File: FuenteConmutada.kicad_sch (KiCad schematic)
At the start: 25 parts, among them J1 Conn_01x02_Socket, J2 Conn_01x03_Socket, U1 MT3608

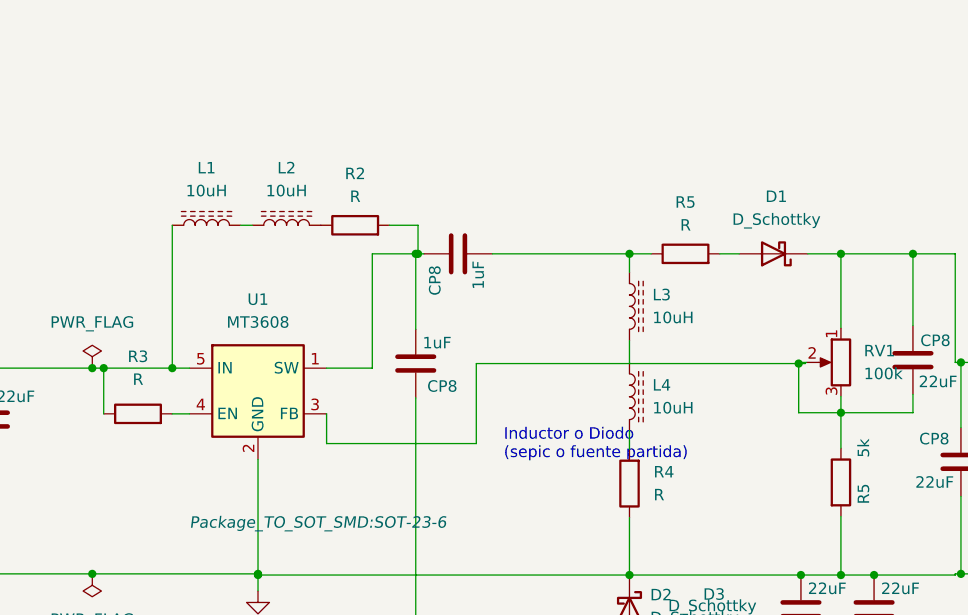
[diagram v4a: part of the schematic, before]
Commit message: Ajustes planos y tracks
Agrandar Margen a 40mils de los planos
Cambiar Rmed de lado del inductor (hacia Vin)
Cambiar Pos Inductores, mas cerca de SW
Aumentar a 50mils todos los tracks que no esten embutidos en planos
Puente en GND/Vfedback para no pasar debajo del SOT23
-Verificar cambios y poner Listo en la wiki
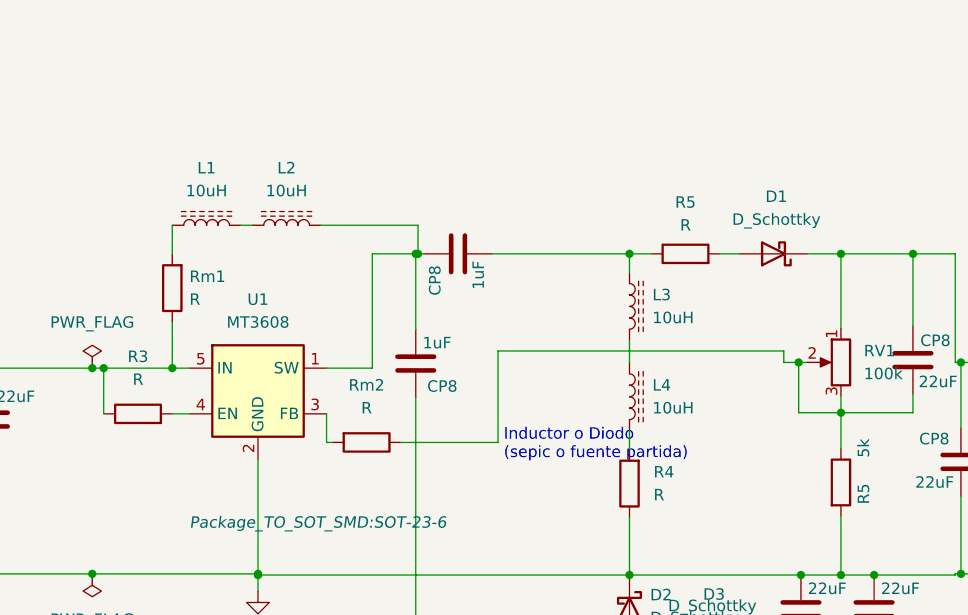
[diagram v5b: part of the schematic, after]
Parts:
- removed R2: R, Resistor_SMD:R_1206_3216Metric_Pad1.30x1.75mm_HandSolder, symbol Device:R
- added Rm1, Rm2: R, Resistor_SMD:R_1206_3216Metric_Pad1.30x1.75mm_HandSolder, symbol Device:R
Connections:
- net Vin: now also Rm1.1; no longer L1.1
- net at CP8.1, CP8.2, U1.1 (SW): now also L2.2
- net at CP8.1, R5.1, RV1.2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: now also Rm2.1; no longer U1.3 (FB)
- new net: Rm2.2, U1.3 (FB)
- new net: L1.1, Rm1.2
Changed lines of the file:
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@@
   (junction (at 94.996 76.2) (diameter 0) (color 0 0 0 0)
   )
-  (junction (at 195.326 75.692) (diameter 0) (color 0 0 0 0)
+  (junction (at 125.73 76.2) (diameter 0) (color 0 0 0 0)
   )
   (junction (at 135.255 99.06) (diameter 0) (color 0 0 0 0)
@@
   (junction (at 116.84 76.2) (diameter 0) (color 0 0 0 0)
   )
-  (junction (at 125.73 76.2) (diameter 0) (color 0 0 0 0)
-  )
   (junction (at 203.708 99.187) (diameter 0) (color 0 0 0 0)
   )
+  (junction (at 195.326 75.565) (diameter 0) (color 0 0 0 0)
+  )
   (junction (at 116.84 99.06) (diameter 0) (color 0 0 0 0)
   )
@@
   (junction (at 213.36 75.565) (diameter 0) (color 0 0 0 0)
   )
-  (wire (pts (xy 195.326 75.692) (xy 195.326 75.565))
+  (wire (pts (xy 161.925 74.295) (xy 161.925 84.455))
     (stroke (width 0) (type default))
   )
@@
     (stroke (width 0) (type default))
   )
-  (wire (pts (xy 159.512 75.692) (xy 195.326 75.692))
-    (stroke (width 0) (type default))
-  )
   (wire (pts (xy 224.917 106.807) (xy 224.917 101.6))
     (stroke (width 0) (type default))
@@
     (stroke (width 0) (type default))
   )
-  (wire (pts (xy 142.875 84.582) (xy 142.875 81.28))
-    (stroke (width 0) (type default))
-  )
   (wire (pts (xy 152.781 71.882) (xy 152.781 63.5))
     (stroke (width 0) (type default))
@@
     (stroke (width 0) (type default))
   )
+  (wire (pts (xy 195.326 75.565) (xy 196.215 75.565))
+    (stroke (width 0) (type default))
+  )
   (wire (pts (xy 94.996 76.2) (xy 105.41 76.2))
     (stroke (width 0) (type default))
@@
     (stroke (width 0) (type default))
   )
+  (wire (pts (xy 125.73 76.2) (xy 127.635 76.2))
+    (stroke (width 0) (type default))
+  )
   (wire (pts (xy 116.84 76.2) (xy 118.11 76.2))
     (stroke (width 0) (type default))
   )
-  (wire (pts (xy 159.512 75.692) (xy 159.512 84.582))
-    (stroke (width 0) (type default))
-  )
   (wire (pts (xy 229.997 96.52) (xy 223.52 96.52))
     (stroke (width 0) (type default))
   )
-  (wire (pts (xy 142.875 84.582) (xy 159.512 84.582))
-    (stroke (width 0) (type default))
-  )
   (wire (pts (xy 200.025 81.153) (xy 200.025 85.09))
     (stroke (width 0) (type default))
@@
     (stroke (width 0) (type default))
   )
+  (wire (pts (xy 142.875 84.455) (xy 143.51 84.455))
+    (stroke (width 0) (type default))
+  )
   (wire (pts (xy 212.725 75.565) (xy 213.36 75.565))
     (stroke (width 0) (type default))
@@
     (stroke (width 0) (type default))
   )
-  (wire (pts (xy 125.73 60.325) (xy 125.73 76.2))
-    (stroke (width 0) (type default))
-  )
-  (wire (pts (xy 195.326 75.692) (xy 195.326 81.153))
+  (wire (pts (xy 195.326 75.565) (xy 195.326 81.153))
+    (stroke (width 0) (type default))
+  )
+  (wire (pts (xy 161.925 74.295) (xy 193.675 74.295))
     (stroke (width 0) (type default))
   )
@@
     (stroke (width 0) (type default))
   )
+  (wire (pts (xy 151.13 84.455) (xy 161.925 84.455))
+    (stroke (width 0) (type default))
+  )
   (wire (pts (xy 208.026 63.5) (xy 212.725 63.5))
     (stroke (width 0) (type default))
@@
     (stroke (width 0) (type default))
   )
+  (wire (pts (xy 125.73 60.325) (xy 125.73 63.5))
+    (stroke (width 0) (type default))
+  )
   (wire (pts (xy 147.955 63.5) (xy 152.781 63.5))
     (stroke (width 0) (type default))
   )
-  (wire (pts (xy 195.326 75.565) (xy 196.215 75.565))
-    (stroke (width 0) (type default))
-  )
   (wire (pts (xy 94.996 98.933) (xy 94.996 99.06))
     (stroke (width 0) (type default))
@@
     (stroke (width 0) (type default))
   )
+  (wire (pts (xy 193.675 74.295) (xy 193.675 75.565))
+    (stroke (width 0) (type default))
+  )
   (wire (pts (xy 94.996 76.2) (xy 94.996 79.375))
     (stroke (width 0) (type default))
@@
     (stroke (width 0) (type default))
   )
-  (wire (pts (xy 125.73 76.2) (xy 127.635 76.2))
+  (wire (pts (xy 118.11 76.2) (xy 125.73 76.2))
     (stroke (width 0) (type default))
   )
@@
     (stroke (width 0) (type default))
   )
-  (wire (pts (xy 196.088 75.692) (xy 195.326 75.692))
-    (stroke (width 0) (type default))
-  )
   (wire (pts (xy 208.026 63.5) (xy 208.026 71.501))
     (stroke (width 0) (type default))
@@
     (stroke (width 0) (type default))
   )
-  (wire (pts (xy 118.11 76.2) (xy 125.73 76.2))
-    (stroke (width 0) (type default))
-  )
   (wire (pts (xy 212.725 63.5) (xy 212.725 75.565))
     (stroke (width 0) (type default))
@@
     (stroke (width 0) (type default))
   )
+  (wire (pts (xy 142.875 81.28) (xy 142.875 84.455))
+    (stroke (width 0) (type default))
+  )
   (wire (pts (xy 176.53 99.187) (xy 195.58 99.187))
     (stroke (width 0) (type default))
@@
     (stroke (width 0) (type default))
   )
-  (wire (pts (xy 149.86 60.325) (xy 153.035 60.325))
+  (wire (pts (xy 142.24 60.325) (xy 153.035 60.325))
     (stroke (width 0) (type default))
   )
@@
     (stroke (width 0) (type default))
   )
+  (wire (pts (xy 125.73 71.12) (xy 125.73 76.2))
+    (stroke (width 0) (type default))
+  )
   (wire (pts (xy 118.11 76.2) (xy 118.11 81.28))
     (stroke (width 0) (type default))
@@
   )
   (wire (pts (xy 176.53 83.185) (xy 176.53 85.217))
+    (stroke (width 0) (type default))
+  )
+  (wire (pts (xy 193.675 75.565) (xy 195.326 75.565))
     (stroke (width 0) (type default))
   )
@@
     )
   )
-  (symbol (lib_id "Device:R") (at 146.05 60.325 90) (unit 1)
+  (symbol (lib_id "Device:R") (at 147.32 84.455 270) (unit 1)
     (in_bom yes) (on_board yes) (dnp no) (fields_autoplaced)
-    (property "Reference" "R2" (at 146.05 54.61 90)
-      (effects (font (size 1.27 1.27)))
-    )
-    (property "Value" "R" (at 146.05 57.15 90)
-      (effects (font (size 1.27 1.27)))
-    )
-    (property "Footprint" "Resistor_SMD:R_1206_3216Metric_Pad1.30x1.75mm_HandSolder" (at 146.05 62.103 90)
-      (effects (font (size 1.27 1.27)) hide)
-    )
-    (property "Datasheet" "~" (at 146.05 60.325 0)
-      (effects (font (size 1.27 1.27)) hide)
-    )
-    (pin "1")
-    (pin "2")
-    (instances
-      (project "FuenteConmutada"
-        (path "/d7444c1b-87b0-4ff7-a57a-a32071ba4b64"
-          (reference "R2") (unit 1)
+    (property "Reference" "Rm2" (at 147.32 78.105 90)
+      (effects (font (size 1.27 1.27)))
+    )
+    (property "Value" "R" (at 147.32 80.645 90)
+      (effects (font (size 1.27 1.27)))
+    )
+    (property "Footprint" "Resistor_SMD:R_1206_3216Metric_Pad1.30x1.75mm_HandSolder" (at 147.32 82.677 90)
+      (effects (font (size 1.27 1.27)) hide)
+    )
+    (property "Datasheet" "~" (at 147.32 84.455 0)
+      (effects (font (size 1.27 1.27)) hide)
+    )
+    (pin "1")
+    (pin "2")
+    (instances
+      (project "FuenteConmutada"
+        (path "/d7444c1b-87b0-4ff7-a57a-a32071ba4b64"
+          (reference "Rm2") (unit 1)
         )
       )
@@
         )
       )
+    )
+  )
+  (symbol (lib_id "Device:R") (at 125.73 67.31 180) (unit 1)
+    (in_bom yes) (on_board yes) (dnp no) (fields_autoplaced)
+    (property "Reference" "Rm1" (at 127.635 66.04 0)
+      (effects (font (size 1.27 1.27)) (justify right))
+    )
+    (property "Value" "R" (at 127.635 68.58 0)
+      (effects (font (size 1.27 1.27)) (justify right))
+    )
+    (property "Footprint" "Resistor_SMD:R_1206_3216Metric_Pad1.30x1.75mm_HandSolder" (at 127.508 67.31 90)
+      (effects (font (size 1.27 1.27)) hide)
+    )
+    (property "Datasheet" "~" (at 125.73 67.31 0)
+      (effects (font (size 1.27 1.27)) hide)
+    )
+    (pin "1")
+    (pin "2")
+    (instances
+      (project "FuenteConmutada"
+        (path "/d7444c1b-87b0-4ff7-a57a-a32071ba4b64"
+          (reference "Rm1") (unit 1)
+        )
+      )
